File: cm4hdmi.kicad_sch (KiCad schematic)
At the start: 8 parts, among them J2 2086581051, U7 AP22653FDZ-7, U8 TPD8S009DSMR

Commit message: board refresh
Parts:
- renumbered C12 to C10, C13 to C11, C11 to C9, R30 to R33, R31 to R34, U7 to U6, U8 to U7
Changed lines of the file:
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@@
   (symbol (lib_id "Power_Protection_Diodes:AP22653FDZ-7") (at 86.36 153.67 0) (unit 1)
     (in_bom yes) (on_board yes)
-    (property "Reference" "U7" (id 0) (at 86.36 144.78 0))
+    (property "Reference" "U6" (id 0) (at 86.36 144.78 0))
     (property "Value" "AP22653FDZ-7" (id 1) (at 86.36 147.32 0))
     (property "Footprint" "Power_Protection_Diodes:Diodes_W-DFN2020-6_A1" (id 2) (at 86.36 167.64 0)
@@
   (symbol (lib_id "Device:R_Small") (at 105.41 153.67 90) (unit 1)
     (in_bom yes) (on_board yes)
-    (property "Reference" "R31" (id 0) (at 107.95 156.21 90)
+    (property "Reference" "R34" (id 0) (at 107.95 156.21 90)
       (effects (font (size 1.27 1.27)) (justify left))
     )
@@
   (symbol (lib_id "Power_Protection_TI:TPD8S009DSMR") (at 227.33 69.85 90) (mirror x) (unit 1)
     (in_bom yes) (on_board yes)
-    (property "Reference" "U8" (id 0) (at 205.74 74.93 90)
+    (property "Reference" "U7" (id 0) (at 205.74 74.93 90)
       (effects (font (size 1.524 1.524)) (justify right))
     )
@@
   (symbol (lib_id "Device:R_Small") (at 86.36 160.02 270) (unit 1)
     (in_bom yes) (on_board yes)
-    (property "Reference" "R30" (id 0) (at 86.36 162.56 90))
+    (property "Reference" "R33" (id 0) (at 86.36 162.56 90))
     (property "Value" "10k" (id 1) (at 86.36 165.1 90))
     (property "Footprint" "Resistor_SMD:R_0402_1005Metric" (id 2) (at 86.36 160.02 0)
@@
   (symbol (lib_id "power:GND") (at 104.14 110.49 0) (unit 1)
     (in_bom yes) (on_board yes) (fields_autoplaced)
-    (property "Reference" "#PWR021" (id 0) (at 104.14 116.84 0)
+    (property "Reference" "#PWR019" (id 0) (at 104.14 116.84 0)
       (effects (font (size 1.27 1.27)) hide)
     )
@@
   (symbol (lib_id "power:GND") (at 248.92 63.5 0) (unit 1)
     (in_bom yes) (on_board yes)
-    (property "Reference" "#PWR023" (id 0) (at 248.92 69.85 0)
+    (property "Reference" "#PWR021" (id 0) (at 248.92 69.85 0)
       (effects (font (size 1.27 1.27)) hide)
     )
@@
   (symbol (lib_id "Device:C_Small") (at 137.16 157.48 0) (unit 1)
     (in_bom yes) (on_board yes)
-    (property "Reference" "C13" (id 0) (at 138.43 156.21 0)
+    (property "Reference" "C11" (id 0) (at 138.43 156.21 0)
       (effects (font (size 1.27 1.27)) (justify left))
     )
@@
   (symbol (lib_id "power:GND") (at 137.16 170.18 0) (unit 1)
     (in_bom yes) (on_board yes)
-    (property "Reference" "#PWR022" (id 0) (at 137.16 176.53 0)
+    (property "Reference" "#PWR020" (id 0) (at 137.16 176.53 0)
       (effects (font (size 1.27 1.27)) hide)
     )
@@
   (symbol (lib_id "Device:C_Small") (at 127 157.48 0) (unit 1)
     (in_bom yes) (on_board yes)
-    (property "Reference" "C12" (id 0) (at 128.27 156.21 0)
+    (property "Reference" "C10" (id 0) (at 128.27 156.21 0)
       (effects (font (size 1.27 1.27)) (justify left))
     )
@@
   (symbol (lib_id "Device:C_Small") (at 57.15 156.21 0) (unit 1)
     (in_bom yes) (on_board yes)
-    (property "Reference" "C11" (id 0) (at 58.42 154.94 0)
-      (effects (font (size 1.27 1.27)) (justify left))
-    )
+    (property "Reference" "C9" (id 0) (at 58.42 154.94 0)
+      (effects (font (size 1.27 1.27)) (justify left))
+    )

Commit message: work on control logic
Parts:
- renumbered R33 to R35, R34 to R36
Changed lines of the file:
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@@
   (symbol (lib_id "Device:R_Small") (at 105.41 153.67 90) (unit 1)
     (in_bom yes) (on_board yes)
-    (property "Reference" "R34" (id 0) (at 107.95 156.21 90)
+    (property "Reference" "R36" (id 0) (at 107.95 156.21 90)
       (effects (font (size 1.27 1.27)) (justify left))
     )
@@
   (symbol (lib_id "Device:R_Small") (at 86.36 160.02 270) (unit 1)
     (in_bom yes) (on_board yes)
-    (property "Reference" "R33" (id 0) (at 86.36 162.56 90))
+    (property "Reference" "R35" (id 0) (at 86.36 162.56 90))
     (property "Value" "10k" (id 1) (at 86.36 165.1 90))
     (property "Footprint" "Resistor_SMD:R_0402_1005Metric" (id 2) (at 86.36 160.02 0)

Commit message: work on control logic
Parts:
- renumbered C9 to C11, C10 to C12, C11 to C13, R35 to R38, R36 to R39, U6 to U7, U7 to U8
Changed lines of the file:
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@@
   (symbol (lib_id "Power_Protection_Diodes:AP22653FDZ-7") (at 86.36 153.67 0) (unit 1)
     (in_bom yes) (on_board yes)
-    (property "Reference" "U6" (id 0) (at 86.36 144.78 0))
+    (property "Reference" "U7" (id 0) (at 86.36 144.78 0))
     (property "Value" "AP22653FDZ-7" (id 1) (at 86.36 147.32 0))
     (property "Footprint" "Power_Protection_Diodes:Diodes_W-DFN2020-6_A1" (id 2) (at 86.36 167.64 0)
@@
   (symbol (lib_id "Device:R_Small") (at 105.41 153.67 90) (unit 1)
     (in_bom yes) (on_board yes)
-    (property "Reference" "R36" (id 0) (at 107.95 156.21 90)
+    (property "Reference" "R39" (id 0) (at 107.95 156.21 90)
       (effects (font (size 1.27 1.27)) (justify left))
     )
@@
   (symbol (lib_id "Power_Protection_TI:TPD8S009DSMR") (at 227.33 69.85 90) (mirror x) (unit 1)
     (in_bom yes) (on_board yes)
-    (property "Reference" "U7" (id 0) (at 205.74 74.93 90)
+    (property "Reference" "U8" (id 0) (at 205.74 74.93 90)
       (effects (font (size 1.524 1.524)) (justify right))
     )
@@
   (symbol (lib_id "Device:R_Small") (at 86.36 160.02 270) (unit 1)
     (in_bom yes) (on_board yes)
-    (property "Reference" "R35" (id 0) (at 86.36 162.56 90))
+    (property "Reference" "R38" (id 0) (at 86.36 162.56 90))
     (property "Value" "10k" (id 1) (at 86.36 165.1 90))
     (property "Footprint" "Resistor_SMD:R_0402_1005Metric" (id 2) (at 86.36 160.02 0)
@@
   (symbol (lib_id "power:GND") (at 104.14 110.49 0) (unit 1)
     (in_bom yes) (on_board yes) (fields_autoplaced)
-    (property "Reference" "#PWR019" (id 0) (at 104.14 116.84 0)
+    (property "Reference" "#PWR020" (id 0) (at 104.14 116.84 0)
       (effects (font (size 1.27 1.27)) hide)
     )
@@
   (symbol (lib_id "power:GND") (at 248.92 63.5 0) (unit 1)
     (in_bom yes) (on_board yes)
-    (property "Reference" "#PWR021" (id 0) (at 248.92 69.85 0)
+    (property "Reference" "#PWR022" (id 0) (at 248.92 69.85 0)
       (effects (font (size 1.27 1.27)) hide)
     )
@@
   (symbol (lib_id "Device:C_Small") (at 137.16 157.48 0) (unit 1)
     (in_bom yes) (on_board yes)
-    (property "Reference" "C11" (id 0) (at 138.43 156.21 0)
+    (property "Reference" "C13" (id 0) (at 138.43 156.21 0)
       (effects (font (size 1.27 1.27)) (justify left))
     )
@@
   (symbol (lib_id "power:GND") (at 137.16 170.18 0) (unit 1)
     (in_bom yes) (on_board yes)
-    (property "Reference" "#PWR020" (id 0) (at 137.16 176.53 0)
+    (property "Reference" "#PWR021" (id 0) (at 137.16 176.53 0)
       (effects (font (size 1.27 1.27)) hide)
     )
@@
   (symbol (lib_id "Device:C_Small") (at 127 157.48 0) (unit 1)
     (in_bom yes) (on_board yes)
-    (property "Reference" "C10" (id 0) (at 128.27 156.21 0)
+    (property "Reference" "C12" (id 0) (at 128.27 156.21 0)
       (effects (font (size 1.27 1.27)) (justify left))
     )
@@
   (symbol (lib_id "Device:C_Small") (at 57.15 156.21 0) (unit 1)
     (in_bom yes) (on_board yes)
-    (property "Reference" "C9" (id 0) (at 58.42 154.94 0)
-      (effects (font (size 1.27 1.27)) (justify left))
-    )
+    (property "Reference" "C11" (id 0) (at 58.42 154.94 0)
+      (effects (font (size 1.27 1.27)) (justify left))
+    )

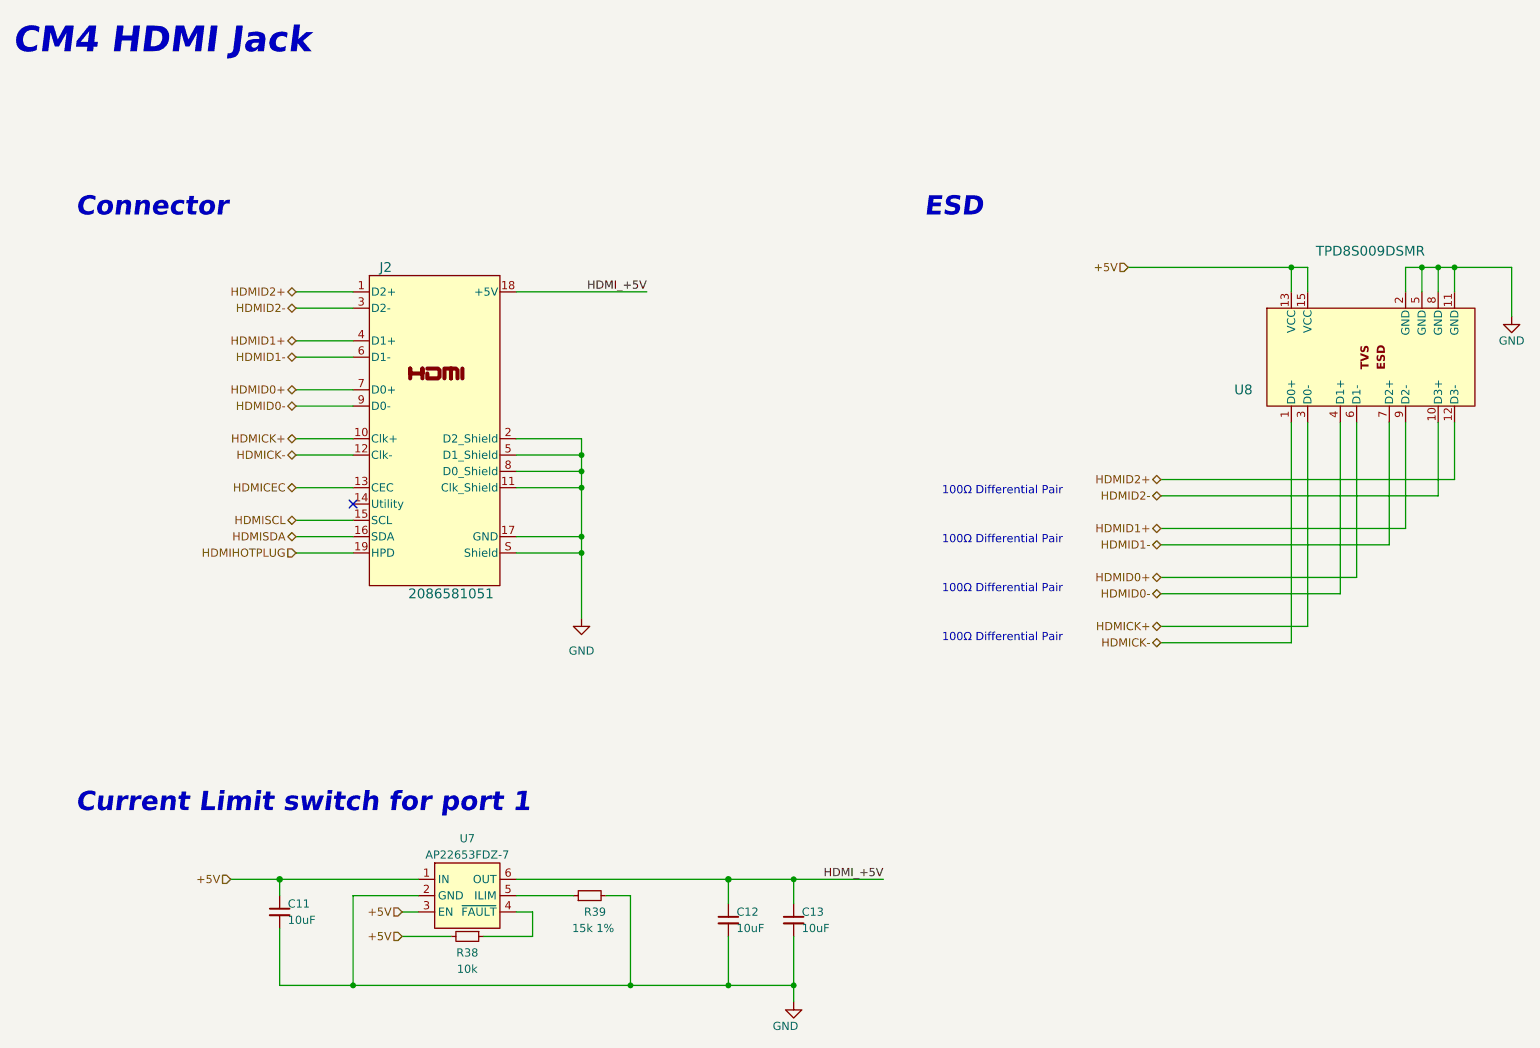
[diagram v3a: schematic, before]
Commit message: connecterized faceplate, refreshed schematic
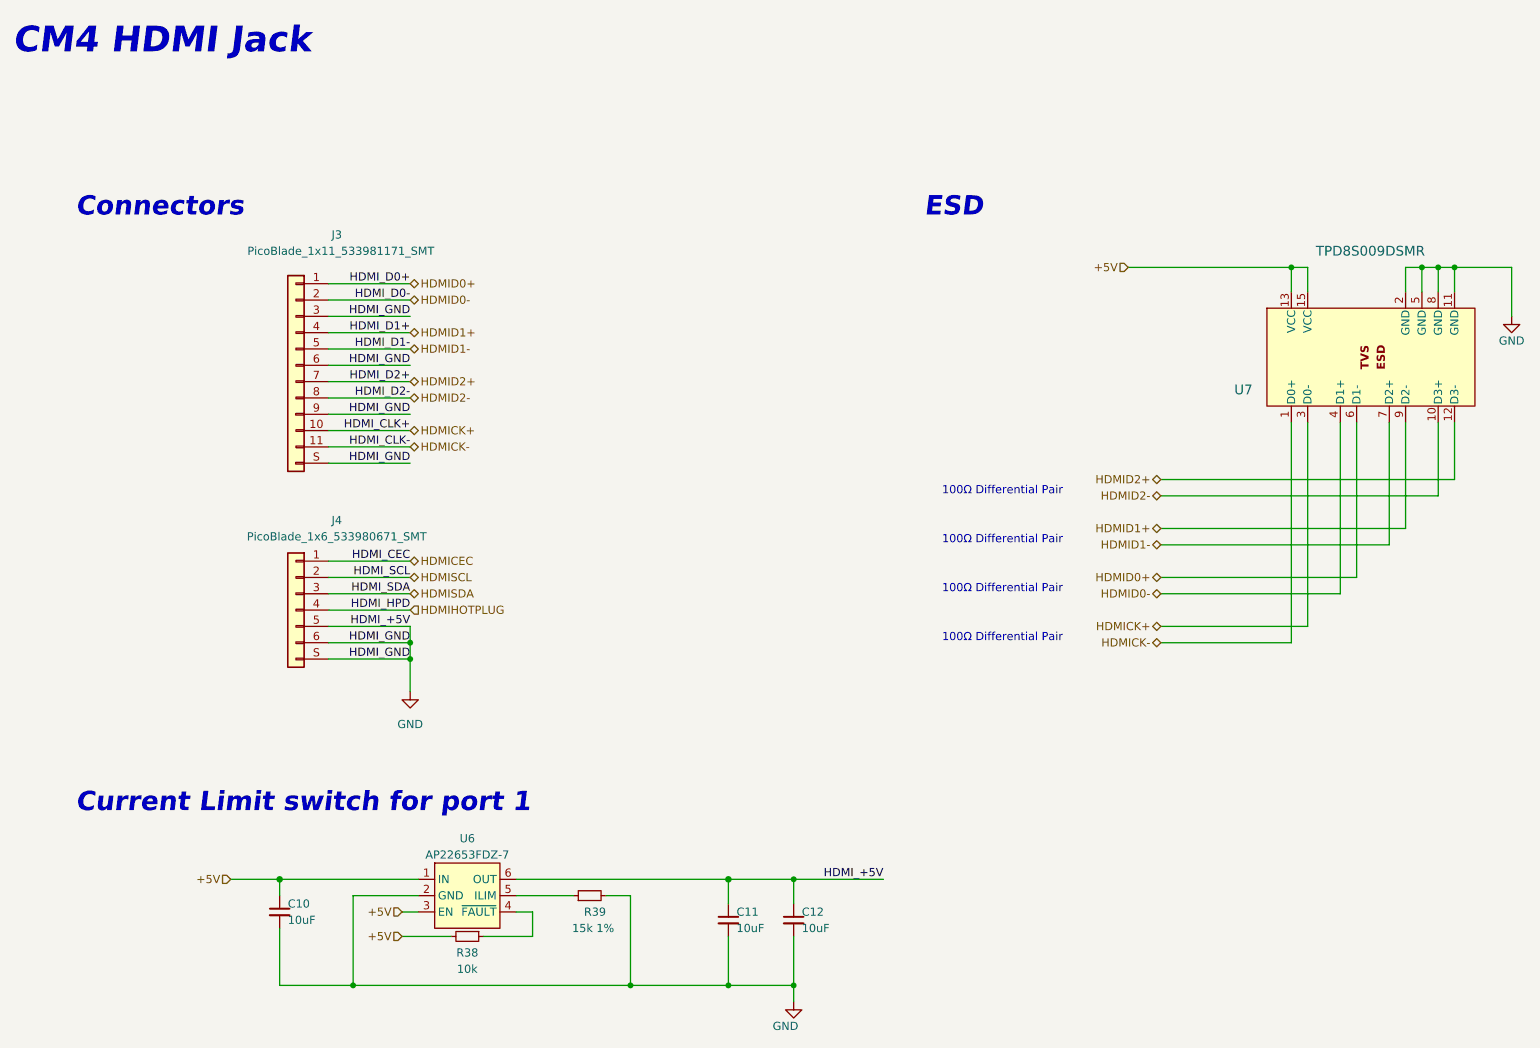
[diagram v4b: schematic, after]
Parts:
- removed J2: 2086581051, Connector_HDMI_Molex:2086581051, symbol Connector_HDMI_Molex:2086581051
- added J3: PicoBlade_1x11_533981171_SMT, Connector_PicoBlade_Molex:MOLEX_533981171, symbol Connector_PicoBlade_Molex:PicoBlade_1x11_533981171_SMT
- added J4: PicoBlade_1x6_533980671_SMT, Connector_PicoBlade_Molex:MOLEX_533980671, symbol Connector_PicoBlade_Molex:PicoBlade_1x6_533980671_SMT
- renumbered C11 to C10, C12 to C11, C13 to C12, U7 to U6, U8 to U7
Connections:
- net HDMI_+5V is gone; now on net GND: C11.1, C12.1, U6.6 (OUT)
- net GND: now also J3.3 (Pin_3), J3.6 (Pin_6), J3.9 (Pin_9), J3.S (SHIELD), J4.5 (Pin_5), J4.6 (Pin_6), J4.S (SHIELD)
- net HDMICEC: now also J4.1 (Pin_1)
- net HDMICK+: now also J3.10 (Pin_10)
- net HDMICK-: now also J3.11 (Pin_11)
- net HDMID0+: now also J3.1 (Pin_1)
- net HDMID0-: now also J3.2 (Pin_2)
- net HDMID1+: now also J3.4 (Pin_4)
- net HDMID1-: now also J3.5 (Pin_5)
- net HDMID2+: now also J3.7 (Pin_7)
- net HDMID2-: now also J3.8 (Pin_8)
- net HDMIHOTPLUG: now also J4.4 (Pin_4)
- net HDMISCL: now also J4.2 (Pin_2)
- net HDMISDA: now also J4.3 (Pin_3)
- no-connect marks 1 -> 0
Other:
- note added: "Connectors"
- note removed: "Connector"

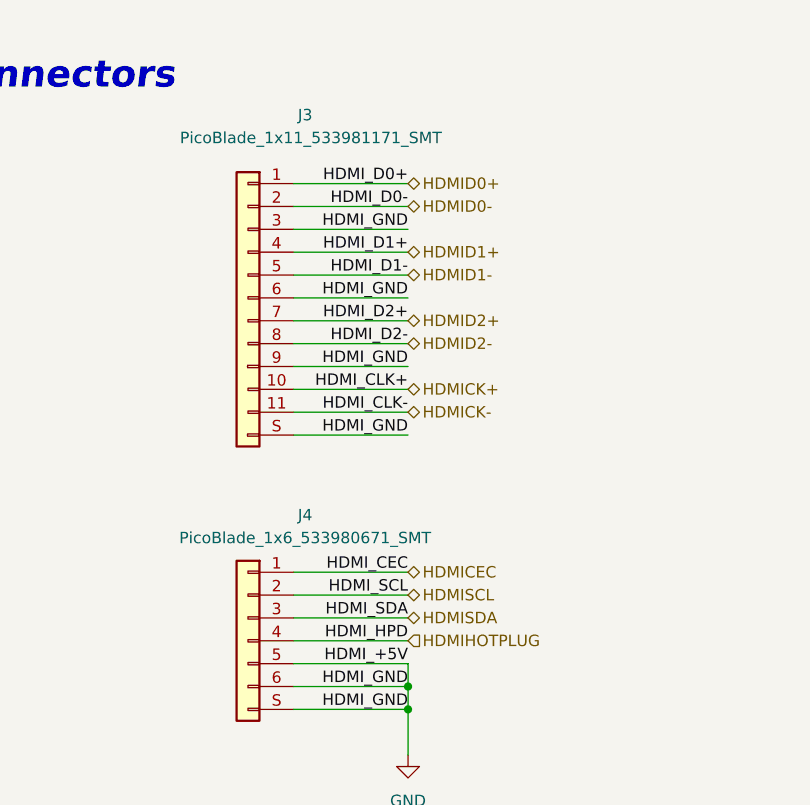
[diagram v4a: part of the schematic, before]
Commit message: placed hdmi conn
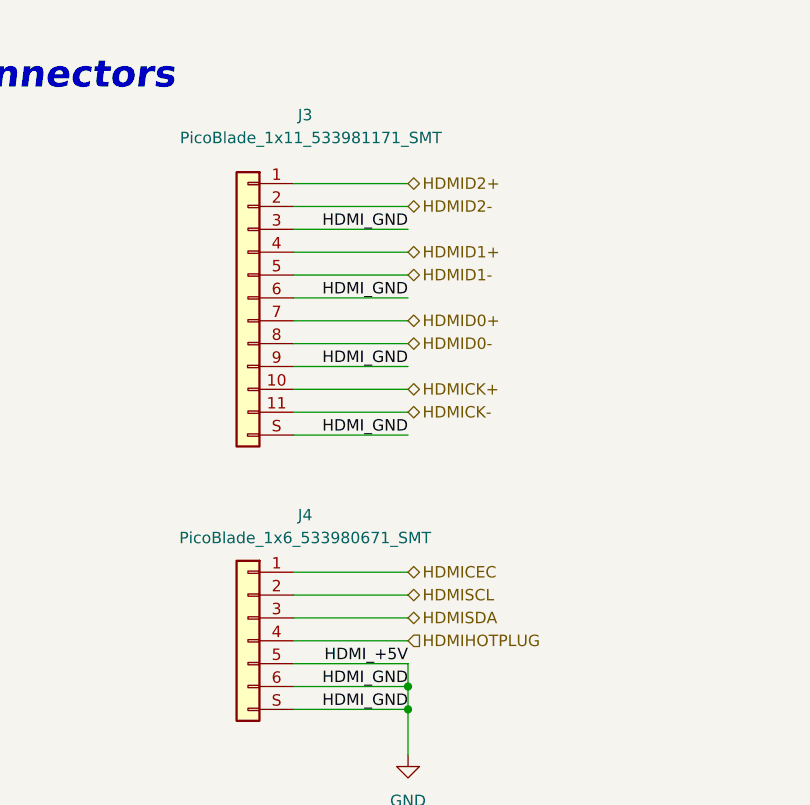
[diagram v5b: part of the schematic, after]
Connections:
- net HDMID0+: now also J3.7 (Pin_7); no longer J3.1 (Pin_1)
- net HDMID0-: now also J3.8 (Pin_8); no longer J3.2 (Pin_2)
- net HDMID2+: now also J3.1 (Pin_1); no longer J3.7 (Pin_7)
- net HDMID2-: now also J3.2 (Pin_2); no longer J3.8 (Pin_8)
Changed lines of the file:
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@@
-    (effects (font (size 1.27 1.27)) (justify right bottom))
-  )
-  (label "HDMI_HPD" (at 77.47 109.22 180)
-    (effects (font (size 1.27 1.27)) (justify right bottom))
-  )
-  (label "HDMI_CLK-" (at 77.47 83.82 180)
-    (effects (font (size 1.27 1.27)) (justify right bottom))
-  )
-  (label "HDMI_D0+" (at 77.47 58.42 180)
     (effects (font (size 1.27 1.27)) (justify right bottom))
   )
   (label "HDMI_GND" (at 77.47 86.36 180)
-    (effects (font (size 1.27 1.27)) (justify right bottom))
-  )
-  (label "HDMI_D1+" (at 77.47 66.04 180)
     (effects (font (size 1.27 1.27)) (justify right bottom))
   )
@@
     (effects (font (size 1.27 1.27)) (justify right bottom))
   )
-  (label "HDMI_SDA" (at 77.47 106.68 180)
-    (effects (font (size 1.27 1.27)) (justify right bottom))
-  )
-  (label "HDMI_CLK+" (at 77.47 81.28 180)
-    (effects (font (size 1.27 1.27)) (justify right bottom))
-  )
   (label "HDMI_GND" (at 77.47 114.3 180)
-    (effects (font (size 1.27 1.27)) (justify right bottom))
-  )
-  (label "HDMI_D1-" (at 77.47 68.58 180)
     (effects (font (size 1.27 1.27)) (justify right bottom))
   )
@@
     (effects (font (size 1.27 1.27)) (justify right bottom))
   )
-  (label "HDMI_D0-" (at 77.47 60.96 180)
-    (effects (font (size 1.27 1.27)) (justify right bottom))
-  )
   (label "HDMI_+5V" (at 151.13 151.13 180)
-    (effects (font (size 1.27 1.27)) (justify right bottom))
-  )
-  (label "HDMI_D2-" (at 77.47 76.2 180)
-    (effects (font (size 1.27 1.27)) (justify right bottom))
-  )
-  (label "HDMI_D2+" (at 77.47 73.66 180)
-    (effects (font (size 1.27 1.27)) (justify right bottom))
-  )
-  (label "HDMI_SCL" (at 77.47 104.14 180)
     (effects (font (size 1.27 1.27)) (justify right bottom))
   )
@@
     (effects (font (size 1.27 1.27)) (justify right bottom))
   )
-  (label "HDMI_CEC" (at 77.47 101.6 180)
-    (effects (font (size 1.27 1.27)) (justify right bottom))
-  )
   (hierarchical_label "HDMIHOTPLUG" (shape input) (at 77.47 109.22 0)
     (effects (font (size 1.27 1.27)) (justify left))
   )
-  (hierarchical_label "HDMID0-" (shape bidirectional) (at 77.47 60.96 0)
+  (hierarchical_label "HDMID0-" (shape bidirectional) (at 77.47 76.2 0)
     (effects (font (size 1.27 1.27)) (justify left))
   )
@@
     (effects (font (size 1.27 1.27)) (justify right))
   )
-  (hierarchical_label "HDMID0+" (shape bidirectional) (at 77.47 58.42 0)
+  (hierarchical_label "HDMID0+" (shape bidirectional) (at 77.47 73.66 0)
     (effects (font (size 1.27 1.27)) (justify left))
   )
@@
     (effects (font (size 1.27 1.27)) (justify right))
   )
-  (hierarchical_label "HDMID2+" (shape bidirectional) (at 77.47 73.66 0)
+  (hierarchical_label "HDMID2+" (shape bidirectional) (at 77.47 58.42 0)
     (effects (font (size 1.27 1.27)) (justify left))
   )
-  (hierarchical_label "HDMID2-" (shape bidirectional) (at 77.47 76.2 0)
+  (hierarchical_label "HDMID2-" (shape bidirectional) (at 77.47 60.96 0)
     (effects (font (size 1.27 1.27)) (justify left))
   )
